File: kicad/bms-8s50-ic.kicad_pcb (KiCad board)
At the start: 2 copper layers, 110 x 60 mm, 163 parts, among them J1 Conn_01x10, J2 UEXT, J3 USB_B_Micro, P1 CONN_01X01, P2 CONN_01X01, P3 CONN_01X01, P4 CONN_01X01, P5 CONN_01X02, Q1 NDS0605, Q10 BSC016N06NS, Q11 BSC016N06NS, Q12 BSC016N06NS, Q13 BSC016N06NS, Q14 BSS138, Q15 BSS138, Q2 NDS0605, Q3 NDS0605, Q4 BSS138, Q5 BSS138, Q6 BSS138, Q7 BSS138, Q8 BSS138, Q9 NDS0605, U1 TPS560430X, U2 TCAN334, U3 STM32F072CBU6, U6 24AA32, U7 ISL94202, Y1 8MHz

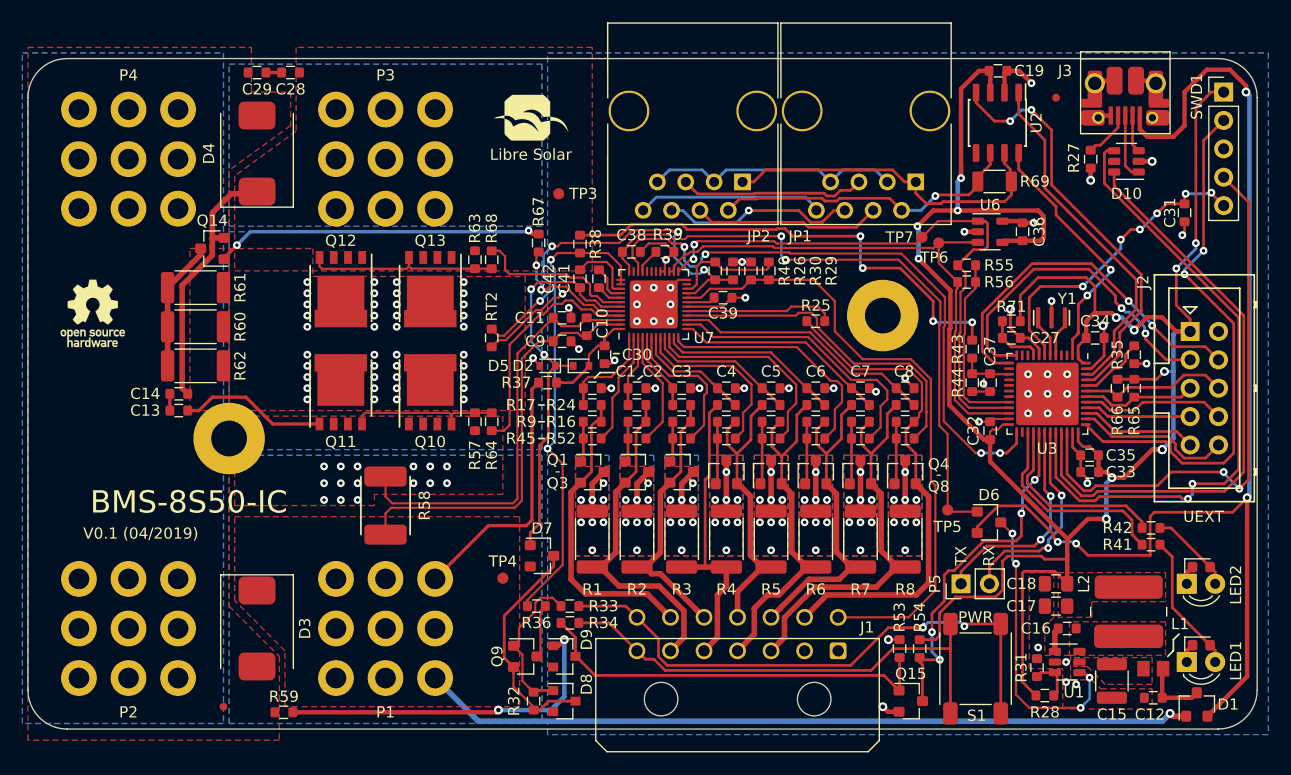
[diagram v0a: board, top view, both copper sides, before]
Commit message: Fix issues found during testing (v0.1.1)
- Add BAT+/- and EXT+/- markings to terminals (#2)
- Change C30 to 470nF (#5)
- Add C20 (47nF) at VC0 pin (#5)
- Add C21 and R72 for proper low-pass filter of VDD (#5)
- Change C39 at VREF to 1uF (#5)
- Add R70: Pull-down for PCHG FET (#5)
- Add R73: Weak pull-down for 5V supply (#6)
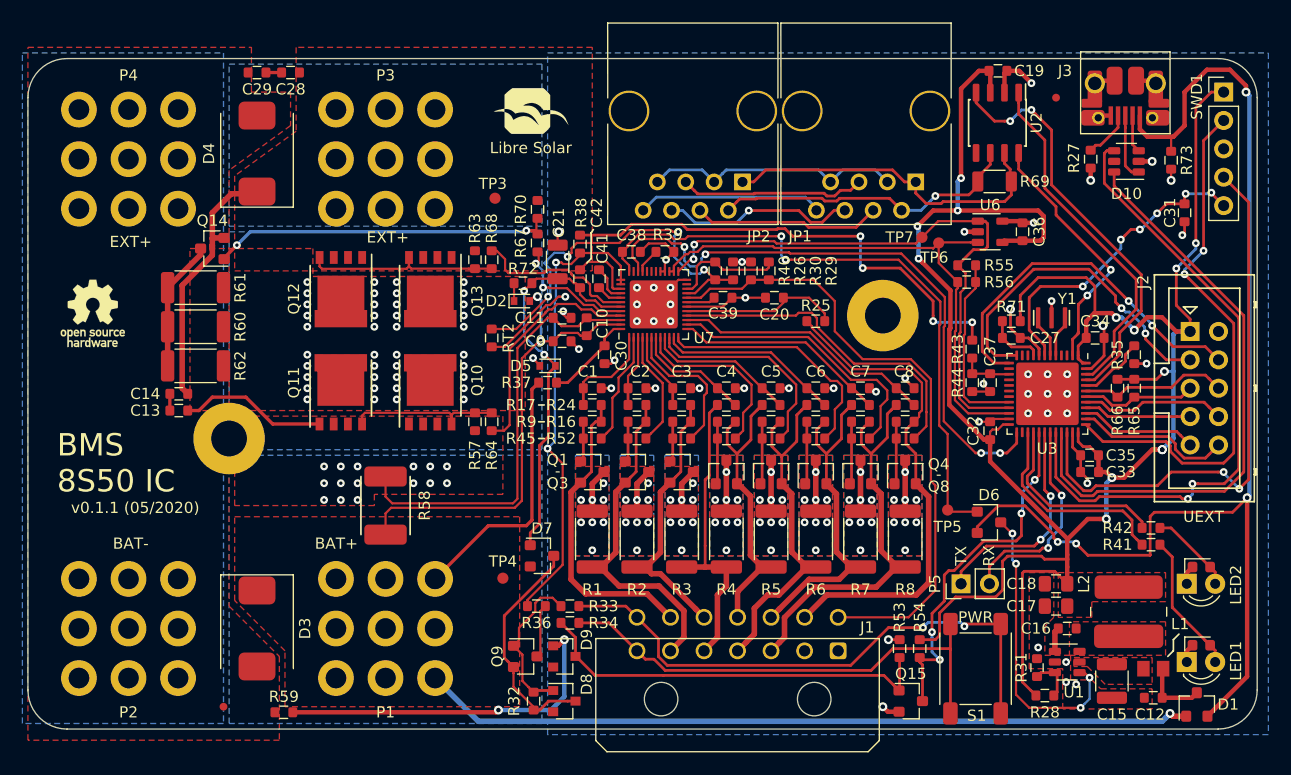
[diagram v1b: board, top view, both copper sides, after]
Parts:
- added C20: 47n, LibreSolar:C_0603_1608, F.Cu at (159.3, 81.4)
- added C21: 4.7u, LibreSolar:C_1206_3216, F.Cu at (139.9, 78.2)
- added R70: 1M, LibreSolar:R_0603_1608, F.Cu at (138.1, 73.5)
- added R72: 4R7, LibreSolar:R_0603_1608, F.Cu at (136.8, 80.1)
- added R73: 330k, LibreSolar:R_0603_1608, F.Cu at (194.8, 69.1)
- C30: value 47n -> 470n
- C39: value 100n -> 1u
- R28: value 54.9k -> 50.5k
- R31: value 10k -> 22k
- moved D2 7.86 mm to (136.7, 81.7)
- moved TP3 5.71 mm to (134.3, 72.5)
- moved LOGO2 0.60 mm to (135.2, 66.7)
- moved R67 0.10 mm to (138.1, 76.5)
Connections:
- net /ISL94202/TEMP0 renamed /ISL94202/TEMPO
- D2 pad 1: /ISL94202/VDD -> Net-(D2-Pad1)
- D2 pad 2: Net-(C30-Pad1) -> /BAT+
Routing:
- net GND: track 137.7 -> 142.9 mm, vias 53 -> 55
- net /BAT+: track 130.2 -> 135.2 mm, vias 1 -> 3
- net Net-(D2-Pad1): track 0.00 -> 1.60 mm
- net Net-(Q14-Pad1): track 29.4 -> 30.9 mm
- net +5V: track 105.6 -> 106.9 mm
- net /ISL94202/VC0: track 13.5 -> 14.4 mm
- net Net-(C30-Pad1): track 8.75 -> 8.14 mm
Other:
- board text added: "2-layer PCB 70µm copper thickness Silkscreen top only"
- board text added: "BAT+"
- board text added: "BAT-"
- board text added: "BMS 8S50 IC"
- board text added: "EXT+"
- board text added: "v0.1.1 (05/2020)"
- board text removed: "BMS-8S50-IC"
- board text removed: "V0.1 (04/2019)"

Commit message: Update to v0.2
- Switch to STM32L452 MCU (STM32F072 has too little RAM for CAN ISO-TP etc.)
- Add CAN termination jumper
- Add CAN bus power supply diodes
- Update CAN connector to match LS.bus spec
- Add interactive BOM and CSV BOM to build directory
- Add additional thermal vias with 0.2mm diameter under MOSFETs
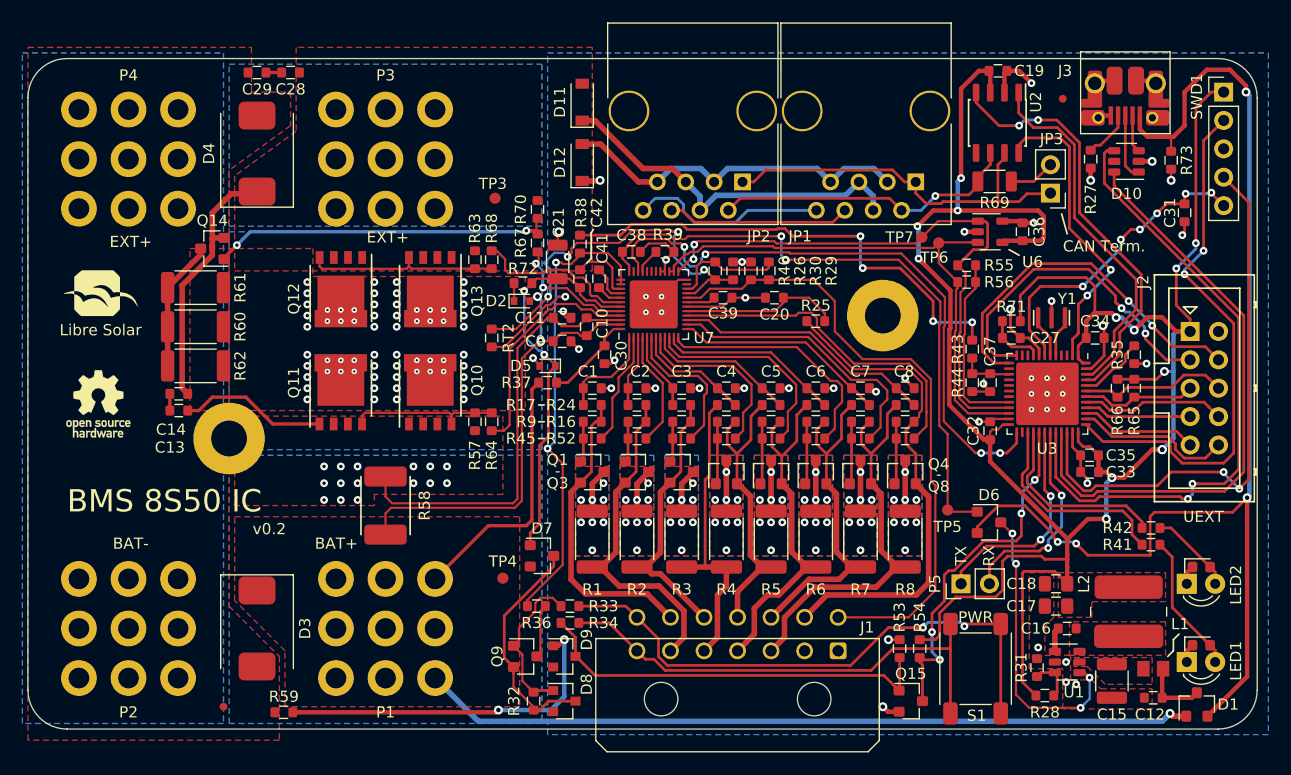
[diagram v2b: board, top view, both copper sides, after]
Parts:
- added D11: NRVTS260ESFT1G, Diode_SMD:D_SOD-123, F.Cu at (142.1, 63.9)
- added D12: NRVTS260ESFT1G, Diode_SMD:D_SOD-123, F.Cu at (142.1, 69.3)
- added JP3: Jumper_NC_Small, Connector_PinHeader_2.54mm:PinHeader_1x02_P2.54mm_Vertical, F.Cu at (184.0, 72.0)
- R58: value 1m -> 0.5m
- R59: value 100 -> 0R
- U3: value STM32F072CBU6 -> STM32L452CCU6
- moved LOGO2 41.8 mm to (96.7, 83.0)
- moved LOGO1 8.12 mm to (98.8, 90.9)
- moved REF** 0.61 mm to (185.1, 63.6)
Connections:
- JP1 pad 3: GND -> /CAN_GND
- JP1 pad 4: Net-(JP1-Pad4) -> /CAN_V+
- JP1 pad 5: Net-(JP1-Pad5) -> /CAN_V+
- JP1 pad 7: GND -> /CAN_GND
- JP1 pad 8: /CAN_V+ -> Net-(JP1-Pad8)
- JP2 pad 3: GND -> /CAN_GND
- JP2 pad 4: Net-(JP1-Pad4) -> /CAN_V+
- JP2 pad 5: Net-(JP1-Pad5) -> /CAN_V+
- JP2 pad 7: GND -> /CAN_GND
- JP2 pad 8: /CAN_V+ -> Net-(JP1-Pad8)
- R69 pad 1: /MCU/CAN_H -> Net-(JP3-Pad2)
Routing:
- net /CAN_GND: track 0.00 -> 31.7 mm
- net GND: track 142.9 -> 121.3 mm, vias 55 -> 52
- net Net-(JP1-Pad8): track 0.00 -> 17.7 mm
- net Net-(JP1-Pad4): track 16.8 -> 0.00 mm
- net Net-(JP1-Pad5): track 16.6 -> 0.00 mm
- net /CAN_V+: track 16.6 -> 33.0 mm
- net /MCU/CAN_STB: track 22.9 -> 27.5 mm
- net /MCU/CAN_H: track 30.9 -> 35.0 mm
- net Net-(JP3-Pad2): track 0.00 -> 4.12 mm
- net /MCU/CAN_TX: track 31.8 -> 33.0 mm
- net Net-(JP1-Pad6): track 17.3 -> 16.4 mm, vias 1 -> 0
- net /ISL94202/CHG+: vias 41 -> 65
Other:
- rule via_min_drill: 0.3 -> 0.2
- rule via_min_size: 0.3 -> 0.2
- board text added: "CAN Term."
- board text added: "v0.2"
- board text removed: "v0.1.1 (05/2020)"
